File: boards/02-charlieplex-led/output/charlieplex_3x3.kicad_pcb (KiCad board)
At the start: 2 copper layers, 50 x 55 mm, 14 parts, among them U1 MCU

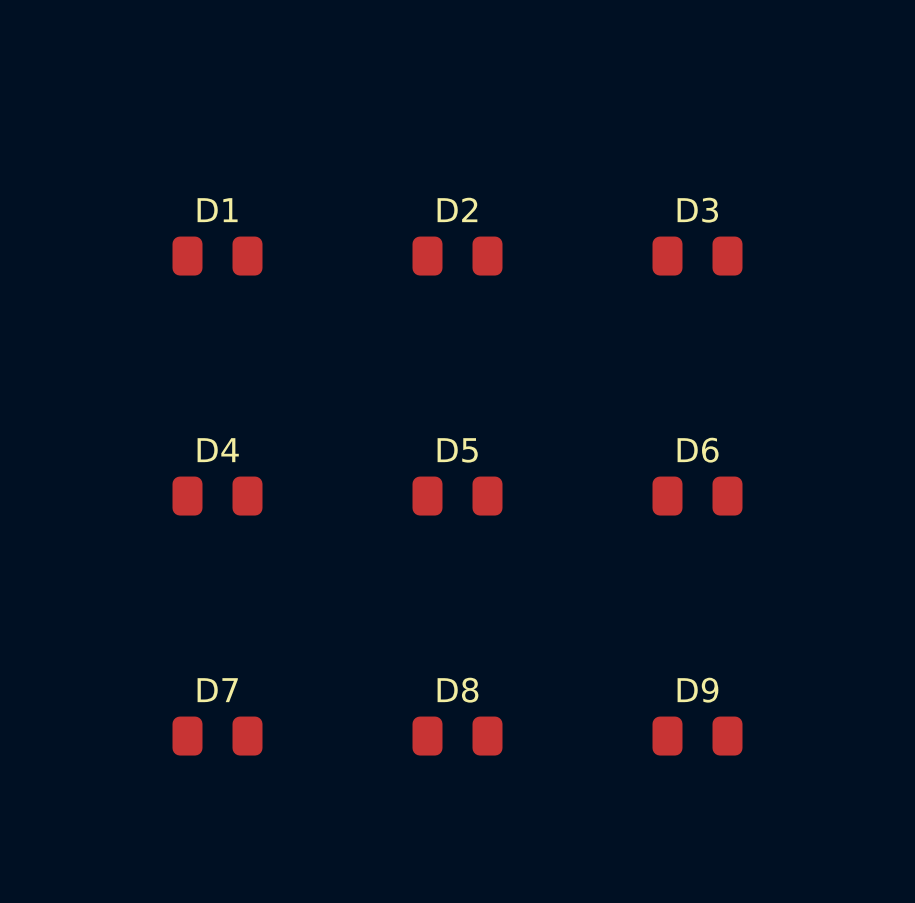
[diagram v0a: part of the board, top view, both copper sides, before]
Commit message: fix(board): Increase LED footprint silkscreen text height to 1.0mm
Update charlieplex LED board to use 1.0mm text height for LED
footprints, matching the JLCPCB minimum recommendation. This resolves
9 DRC warnings that were flagged for text height below 1.0mm.

Changes:
- Update generate_pcb.py LED footprint text from 0.8mm to 1.0mm
- Increase text thickness from 0.12 to 0.15 for consistency
- Regenerate charlieplex_3x3.kicad_pcb with new font sizes
- Regenerate charlieplex_3x3_routed.kicad_pcb with new font sizes

Closes #859

Co-Authored-By: Claude Opus 4.5 <noreply@anthropic.com>
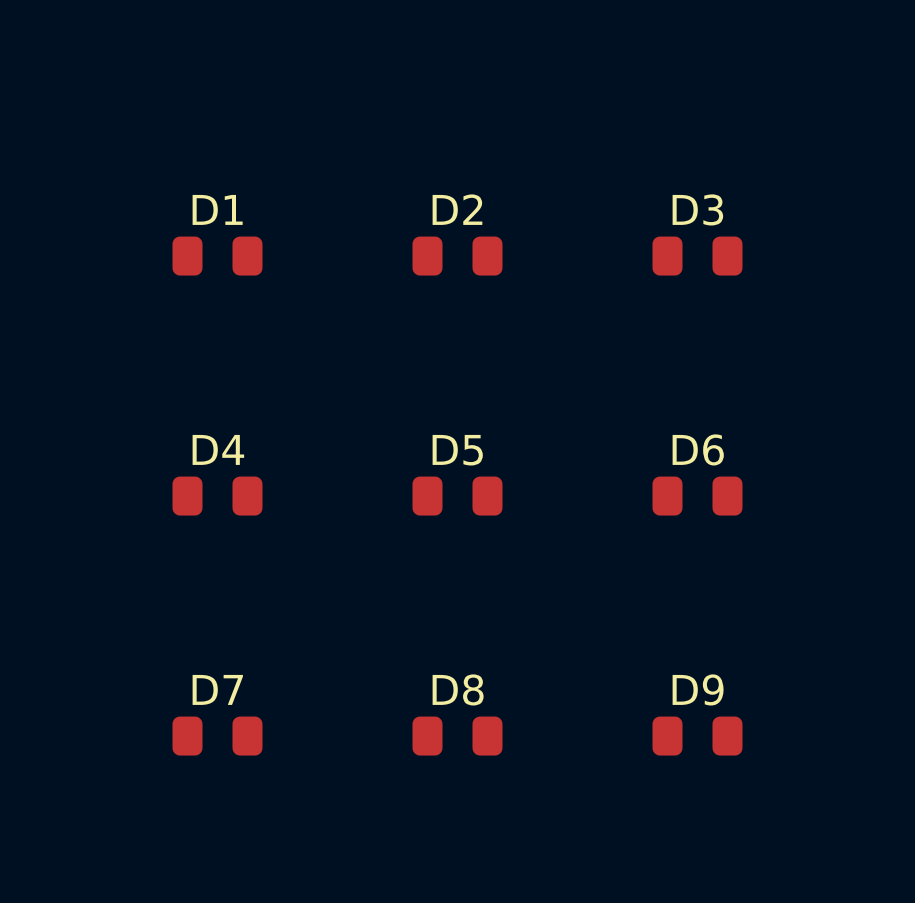
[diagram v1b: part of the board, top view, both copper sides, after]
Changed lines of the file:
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@@
     (at 117.0 110.0)
     (fp_text reference "D1" (at 0 -1.5) (layer "F.SilkS")
-      (effects (font (size 0.8 0.8) (thickness 0.12)))
+      (effects (font (size 1 1) (thickness 0.15)))
     )
     (fp_text value "LED" (at 0 1.5) (layer "F.Fab")
-      (effects (font (size 0.8 0.8) (thickness 0.12)))
+      (effects (font (size 1 1) (thickness 0.15)))
     )
     (pad "1" smd roundrect (at -1.0 0) (size 1.0 1.3) (layers "F.Cu" "F.Paste" "F.Mask") (roundrect_rratio 0.25) (net 6 "NODE_B"))
@@
     (at 125.0 110.0)
     (fp_text reference "D2" (at 0 -1.5) (layer "F.SilkS")
-      (effects (font (size 0.8 0.8) (thickness 0.12)))
+      (effects (font (size 1 1) (thickness 0.15)))
     )
     (fp_text value "LED" (at 0 1.5) (layer "F.Fab")
-      (effects (font (size 0.8 0.8) (thickness 0.12)))
+      (effects (font (size 1 1) (thickness 0.15)))
     )
     (pad "1" smd roundrect (at -1.0 0) (size 1.0 1.3) (layers "F.Cu" "F.Paste" "F.Mask") (roundrect_rratio 0.25) (net 5 "NODE_A"))
@@
     (at 133.0 110.0)
     (fp_text reference "D3" (at 0 -1.5) (layer "F.SilkS")
-      (effects (font (size 0.8 0.8) (thickness 0.12)))
+      (effects (font (size 1 1) (thickness 0.15)))
     )
     (fp_text value "LED" (at 0 1.5) (layer "F.Fab")
-      (effects (font (size 0.8 0.8) (thickness 0.12)))
+      (effects (font (size 1 1) (thickness 0.15)))
     )
     (pad "1" smd roundrect (at -1.0 0) (size 1.0 1.3) (layers "F.Cu" "F.Paste" "F.Mask") (roundrect_rratio 0.25) (net 7 "NODE_C"))
@@
     (at 117.0 118.0)
     (fp_text reference "D4" (at 0 -1.5) (layer "F.SilkS")
-      (effects (font (size 0.8 0.8) (thickness 0.12)))
+      (effects (font (size 1 1) (thickness 0.15)))
     )
     (fp_text value "LED" (at 0 1.5) (layer "F.Fab")
-      (effects (font (size 0.8 0.8) (thickness 0.12)))
+      (effects (font (size 1 1) (thickness 0.15)))
     )
     (pad "1" smd roundrect (at -1.0 0) (size 1.0 1.3) (layers "F.Cu" "F.Paste" "F.Mask") (roundrect_rratio 0.25) (net 5 "NODE_A"))
@@
     (at 125.0 118.0)
     (fp_text reference "D5" (at 0 -1.5) (layer "F.SilkS")
-      (effects (font (size 0.8 0.8) (thickness 0.12)))
+      (effects (font (size 1 1) (thickness 0.15)))
     )
     (fp_text value "LED" (at 0 1.5) (layer "F.Fab")
-      (effects (font (size 0.8 0.8) (thickness 0.12)))
+      (effects (font (size 1 1) (thickness 0.15)))
     )
     (pad "1" smd roundrect (at -1.0 0) (size 1.0 1.3) (layers "F.Cu" "F.Paste" "F.Mask") (roundrect_rratio 0.25) (net 8 "NODE_D"))
@@
     (at 133.0 118.0)
     (fp_text reference "D6" (at 0 -1.5) (layer "F.SilkS")
-      (effects (font (size 0.8 0.8) (thickness 0.12)))
+      (effects (font (size 1 1) (thickness 0.15)))
     )
     (fp_text value "LED" (at 0 1.5) (layer "F.Fab")
-      (effects (font (size 0.8 0.8) (thickness 0.12)))
+      (effects (font (size 1 1) (thickness 0.15)))
     )
     (pad "1" smd roundrect (at -1.0 0) (size 1.0 1.3) (layers "F.Cu" "F.Paste" "F.Mask") (roundrect_rratio 0.25) (net 5 "NODE_A"))
@@
     (at 117.0 126.0)
     (fp_text reference "D7" (at 0 -1.5) (layer "F.SilkS")
-      (effects (font (size 0.8 0.8) (thickness 0.12)))
+      (effects (font (size 1 1) (thickness 0.15)))
     )
     (fp_text value "LED" (at 0 1.5) (layer "F.Fab")
-      (effects (font (size 0.8 0.8) (thickness 0.12)))
+      (effects (font (size 1 1) (thickness 0.15)))
     )
     (pad "1" smd roundrect (at -1.0 0) (size 1.0 1.3) (layers "F.Cu" "F.Paste" "F.Mask") (roundrect_rratio 0.25) (net 7 "NODE_C"))
@@
     (at 125.0 126.0)
     (fp_text reference "D8" (at 0 -1.5) (layer "F.SilkS")
-      (effects (font (size 0.8 0.8) (thickness 0.12)))
+      (effects (font (size 1 1) (thickness 0.15)))
     )
     (fp_text value "LED" (at 0 1.5) (layer "F.Fab")
-      (effects (font (size 0.8 0.8) (thickness 0.12)))
+      (effects (font (size 1 1) (thickness 0.15)))
     )
     (pad "1" smd roundrect (at -1.0 0) (size 1.0 1.3) (layers "F.Cu" "F.Paste" "F.Mask") (roundrect_rratio 0.25) (net 6 "NODE_B"))
@@
     (at 133.0 126.0)
     (fp_text reference "D9" (at 0 -1.5) (layer "F.SilkS")
-      (effects (font (size 0.8 0.8) (thickness 0.12)))
+      (effects (font (size 1 1) (thickness 0.15)))
     )
     (fp_text value "LED" (at 0 1.5) (layer "F.Fab")
-      (effects (font (size 0.8 0.8) (thickness 0.12)))
+      (effects (font (size 1 1) (thickness 0.15)))
     )
     (pad "1" smd roundrect (at -1.0 0) (size 1.0 1.3) (layers "F.Cu" "F.Paste" "F.Mask") (roundrect_rratio 0.25) (net 8 "NODE_D"))

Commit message: fix(boards): connect unused MCU pins to GND in boards 02 and 03
Unused MCU digital input pins were left without net assignments in the
PCB generators, producing pads with no net clause in the KiCad PCB
files. JLCPCB's automated review flags these unconnected pads and holds
orders for clarification. Connect all unused inputs to GND -- standard
practice that prevents floating inputs and eliminates review holds.

Board 02: pins 5, 6 (GND net 10)
Board 03: pins 5, 6, 18, 19, 20, 21, 22, 31 (GND net 3)

Co-Authored-By: Claude Opus 4.6 <noreply@anthropic.com>
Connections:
- U1 pad 5: (no net) -> GND
- U1 pad 6: (no net) -> GND
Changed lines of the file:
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@@
     (pad "3" thru_hole rect (at -3.810 1.270) (size 1.6 1.6) (drill 0.8) (layers "*.Cu" "*.Mask") (net 3 "LINE_C"))
     (pad "4" thru_hole rect (at -3.810 3.810) (size 1.6 1.6) (drill 0.8) (layers "*.Cu" "*.Mask") (net 4 "LINE_D"))
-    (pad "5" thru_hole oval (at 3.810 3.810) (size 1.6 1.6) (drill 0.8) (layers "*.Cu" "*.Mask") )
-    (pad "6" thru_hole oval (at 3.810 1.270) (size 1.6 1.6) (drill 0.8) (layers "*.Cu" "*.Mask") )
+    (pad "5" thru_hole oval (at 3.810 3.810) (size 1.6 1.6) (drill 0.8) (layers "*.Cu" "*.Mask") (net 10 "GND"))
+    (pad "6" thru_hole oval (at 3.810 1.270) (size 1.6 1.6) (drill 0.8) (layers "*.Cu" "*.Mask") (net 10 "GND"))
     (pad "7" thru_hole oval (at 3.810 -1.270) (size 1.6 1.6) (drill 0.8) (layers "*.Cu" "*.Mask") (net 9 "VCC"))
     (pad "8" thru_hole oval (at 3.810 -3.810) (size 1.6 1.6) (drill 0.8) (layers "*.Cu" "*.Mask") (net 10 "GND"))
